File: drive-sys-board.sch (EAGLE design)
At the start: 34 parts, among them J2 APP_2POS_CONFIG12V_HORIZ, U1 OKI-78SR-5/1.5-W36HC, U2 MAX232D, U3 MAX232D, U4 MAX232D

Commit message: Finished routing
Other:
- note removed: "Serial Channel Motor Label Serial2 RR Serial3 FR Serial4 MR Serial5 ML Serial6 FL Serial7 RL"
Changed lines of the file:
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@@
 <text x="-50.8" y="68.58" size="2.54" layer="97">Serial4</text>
 <text x="-50.8" y="12.7" size="2.54" layer="97">Serial6</text>
-<text x="38.1" y="50.8" size="1.778" layer="97">Serial Channel        Motor Label
-     Serial2                   RR
-     Serial3                   FR
-     Serial4                   MR
-     Serial5                   ML
-     Serial6                   FL
-     Serial7                   RL</text>
 </plain>
 <instances>

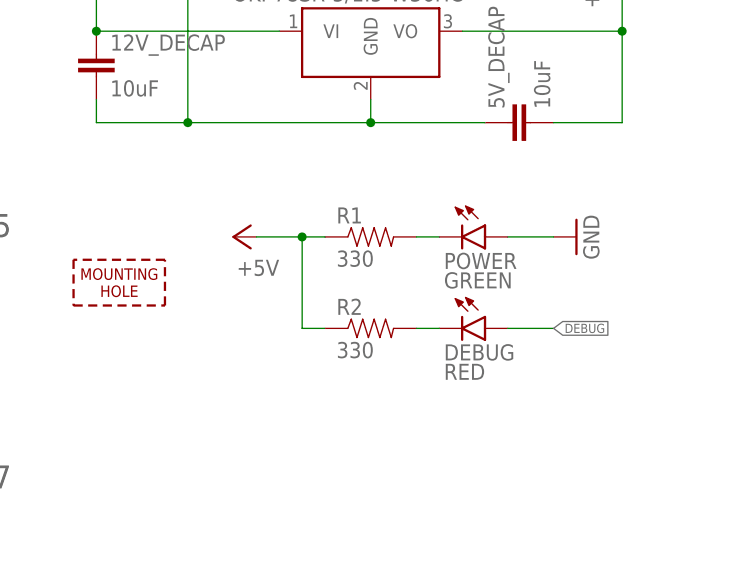
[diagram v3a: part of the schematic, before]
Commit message: Changes from 2nd Review
- changed led direction
- changes led schematic
- moved vias above max232
- thickened 12v line
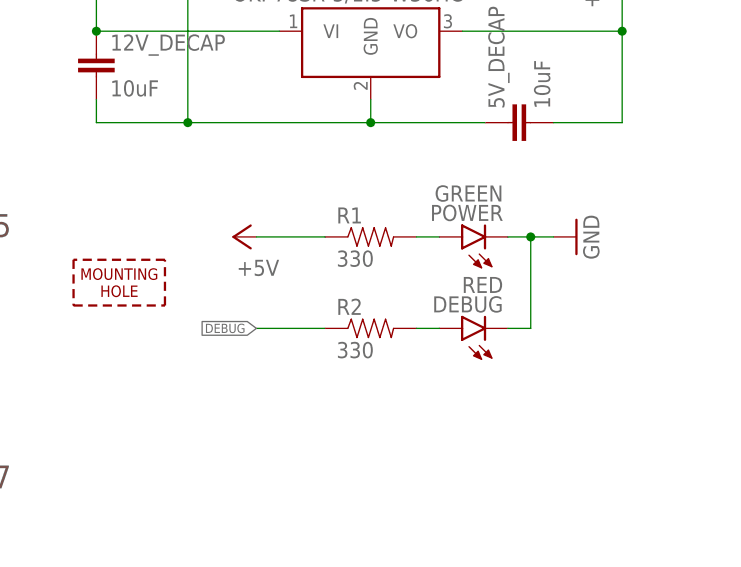
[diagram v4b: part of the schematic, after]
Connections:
- net +5V: no longer R2.1
- net DEBUG: now also R2.1; no longer DEBUG.A
- net GND: now also DEBUG.C, POWER.C; no longer POWER.A
- net N$10: now also DEBUG.A; no longer DEBUG.C
- net N$17: now also POWER.A; no longer POWER.C
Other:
- moved on the sheet: DEBUG, POWER
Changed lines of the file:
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@@
 <instance part="GND10" gate="1" x="-111.76" y="-68.58"/>
 <instance part="P+6" gate="1" x="-15.24" y="-68.58" rot="R90"/>
-<instance part="POWER" gate="G$1" x="12.7" y="-68.58" rot="R270"/>
-<instance part="DEBUG" gate="G$1" x="12.7" y="-78.74" rot="R270"/>
+<instance part="POWER" gate="G$1" x="10.16" y="-68.58" rot="R90"/>
+<instance part="DEBUG" gate="G$1" x="10.16" y="-78.74" rot="R90"/>
 <instance part="GND11" gate="1" x="22.86" y="-68.58" rot="R90"/>
 <instance part="R1" gate="G$1" x="0" y="-68.58"/>
@@
 </segment>
 <segment>
-<wire x1="20.32" y1="-68.58" x2="15.24" y2="-68.58" width="0.1524" layer="91"/>
-<pinref part="POWER" gate="G$1" pin="A"/>
+<pinref part="POWER" gate="G$1" pin="C"/>
 <pinref part="GND11" gate="1" pin="GND"/>
+<wire x1="15.24" y1="-68.58" x2="17.78" y2="-68.58" width="0.1524" layer="91"/>
+<pinref part="DEBUG" gate="G$1" pin="C"/>
+<wire x1="17.78" y1="-68.58" x2="20.32" y2="-68.58" width="0.1524" layer="91"/>
+<wire x1="15.24" y1="-78.74" x2="17.78" y2="-78.74" width="0.1524" layer="91"/>
+<wire x1="17.78" y1="-78.74" x2="17.78" y2="-68.58" width="0.1524" layer="91"/>
+<junction x="17.78" y="-68.58"/>
 </segment>
 </net>
@@
 <pinref part="R1" gate="G$1" pin="1"/>
 <pinref part="P+6" gate="1" pin="+5V"/>
-<wire x1="-12.7" y1="-68.58" x2="-7.62" y2="-68.58" width="0.1524" layer="91"/>
-<pinref part="R2" gate="G$1" pin="1"/>
-<wire x1="-7.62" y1="-68.58" x2="-5.08" y2="-68.58" width="0.1524" layer="91"/>
-<wire x1="-5.08" y1="-78.74" x2="-7.62" y2="-78.74" width="0.1524" layer="91"/>
-<wire x1="-7.62" y1="-78.74" x2="-7.62" y2="-68.58" width="0.1524" layer="91"/>
-<junction x="-7.62" y="-68.58"/>
+<wire x1="-12.7" y1="-68.58" x2="-5.08" y2="-68.58" width="0.1524" layer="91"/>
 </segment>
 </net>
@@
 </segment>
 <segment>
+<pinref part="R2" gate="G$1" pin="1"/>
+<wire x1="-5.08" y1="-78.74" x2="-12.7" y2="-78.74" width="0.1524" layer="91"/>
+<label x="-12.7" y="-78.74" size="1.016" layer="95" rot="R180" xref="yes"/>
+</segment>
+</net>
+<net name="N$17" class="0">
+<segment>
+<pinref part="R1" gate="G$1" pin="2"/>
+<pinref part="POWER" gate="G$1" pin="A"/>
+<wire x1="7.62" y1="-68.58" x2="5.08" y2="-68.58" width="0.1524" layer="91"/>
+</segment>
+</net>
+<net name="N$10" class="0">
+<segment>
+<pinref part="R2" gate="G$1" pin="2"/>
 <pinref part="DEBUG" gate="G$1" pin="A"/>
-<wire x1="15.24" y1="-78.74" x2="20.32" y2="-78.74" width="0.1524" layer="91"/>
-<label x="20.32" y="-78.74" size="1.016" layer="95" xref="yes"/>
-</segment>
-</net>
-<net name="N$10" class="0">
-<segment>
-<pinref part="DEBUG" gate="G$1" pin="C"/>
-<pinref part="R2" gate="G$1" pin="2"/>
-<wire x1="5.08" y1="-78.74" x2="7.62" y2="-78.74" width="0.1524" layer="91"/>
-</segment>
-</net>
-<net name="N$17" class="0">
-<segment>
-<pinref part="POWER" gate="G$1" pin="C"/>
-<pinref part="R1" gate="G$1" pin="2"/>
-<wire x1="5.08" y1="-68.58" x2="7.62" y2="-68.58" width="0.1524" layer="91"/>
-</segment>
-</net>
+<wire x1="7.62" y1="-78.74" x2="5.08" y2="-78.74" width="0.1524" layer="91"/>
+</segment>
+</net>

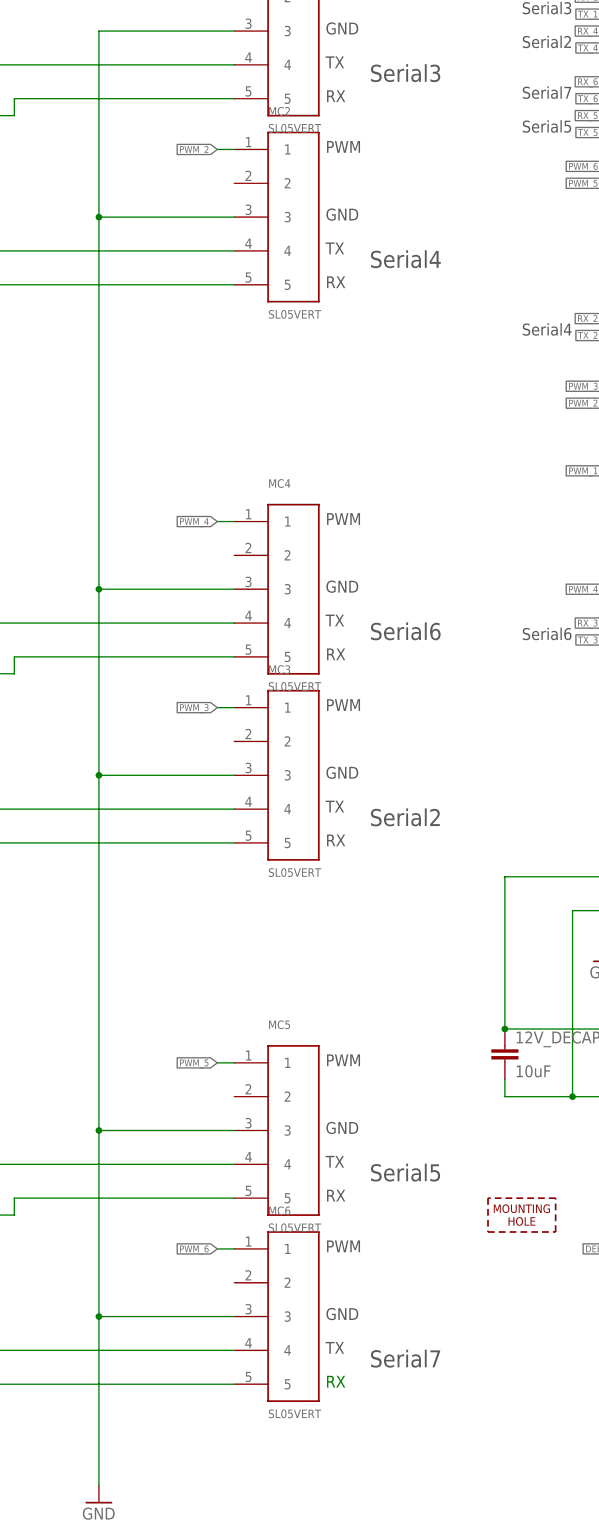
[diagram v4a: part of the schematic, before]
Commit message: Modified 2017 Drive Board for BOD 2018
-Switched all vertical SL connectors to horizontal connectors.
-Moved horizontal connectors to top of board so that there are only
connectors on the top and right side of the board.
-Extended the bottom of the board out further by ~0.6 inches in order to
place .08 inch diameter mounting holes.
-Moved ICs and other passives connected to vertical SL connectors
towards the middle of the board to keep components organized on the
board.
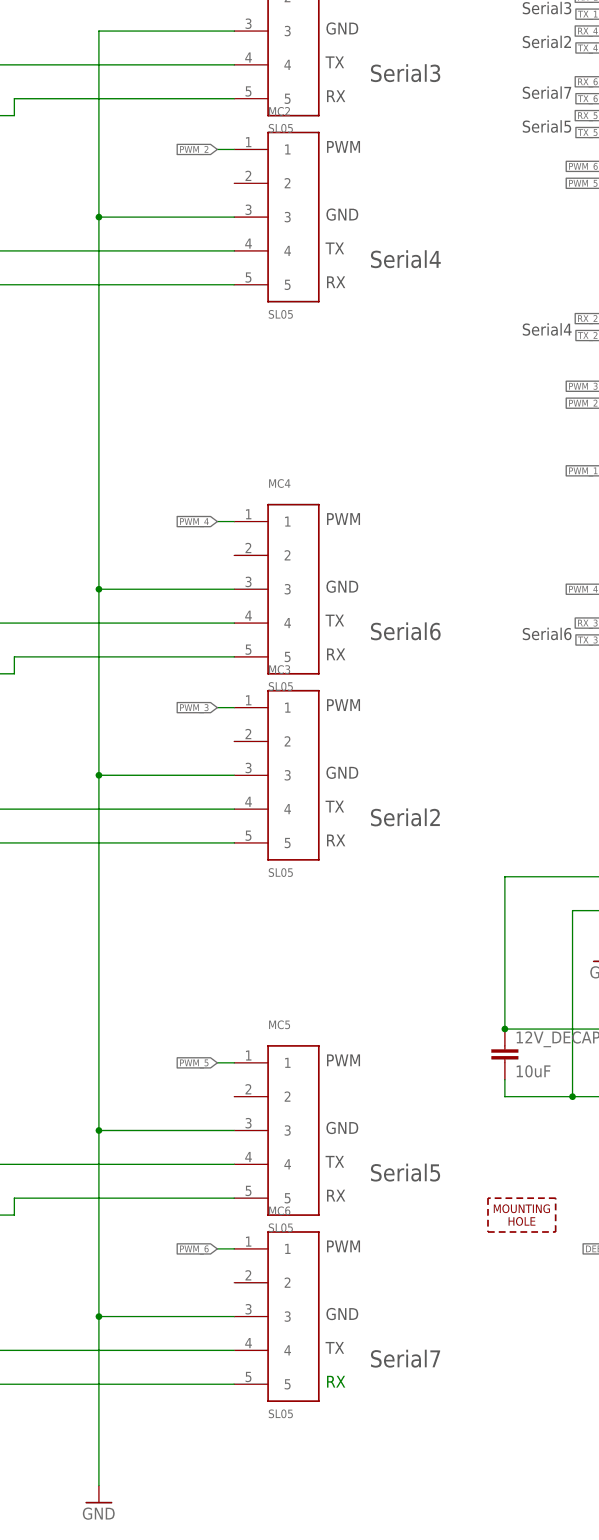
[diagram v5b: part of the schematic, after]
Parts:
- MC1, MC2, MC3, MC4, MC5, MC6: value SL05VERT -> SL05; device MRDT-Connectors:SL05VERT -> MRDT-Connectors:SL05
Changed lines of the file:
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@@
 <?xml version="1.0" encoding="utf-8"?>
 <!DOCTYPE eagle SYSTEM "eagle.dtd">
-<eagle version="7.7.0">
+<eagle version="7.6.0">
 <drawing>
 <settings>
@@
 <part name="C4_3" library="SparkFun-Capacitors" deviceset="CAP" device="0805" value="1uF"/>
 <part name="C5_3" library="SparkFun-Capacitors" deviceset="CAP" device="0805" value="1uF"/>
-<part name="MC1" library="MRDT-Connectors" deviceset="SL05" device="VERT"/>
-<part name="MC2" library="MRDT-Connectors" deviceset="SL05" device="VERT"/>
-<part name="MC4" library="MRDT-Connectors" deviceset="SL05" device="VERT"/>
-<part name="MC3" library="MRDT-Connectors" deviceset="SL05" device="VERT"/>
-<part name="MC5" library="MRDT-Connectors" deviceset="SL05" device="VERT"/>
-<part name="MC6" library="MRDT-Connectors" deviceset="SL05" device="VERT"/>
+<part name="MC1" library="MRDT-Connectors" deviceset="SL05" device="" value="SL05"/>
+<part name="MC2" library="MRDT-Connectors" deviceset="SL05" device="" value="SL05"/>
+<part name="MC4" library="MRDT-Connectors" deviceset="SL05" device="" value="SL05"/>
+<part name="MC3" library="MRDT-Connectors" deviceset="SL05" device="" value="SL05"/>
+<part name="MC5" library="MRDT-Connectors" deviceset="SL05" device="" value="SL05"/>
+<part name="MC6" library="MRDT-Connectors" deviceset="SL05" device="" value="SL05"/>
 <part name="GND2" library="supply1" deviceset="GND" device=""/>
 <part name="5V_DECAP" library="SparkFun-Capacitors" deviceset="CAP" device="0805" value="10uF"/>
